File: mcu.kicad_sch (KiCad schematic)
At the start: 9 parts, among them J2 BOOT SEL, SW1 Reset Switch, U2 STM32F030F4Px

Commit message: feat: added footprints for the 5.1k resistors
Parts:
- C7: footprint Capacitor_SMD:C_0805_2012Metric_Pad1.18x1.45mm_HandSolder -> Capacitor_SMD:C_0603_1608Metric_Pad1.08x0.95mm_HandSolder
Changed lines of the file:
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@@
 			)
 		)
-		(property "Footprint" "Capacitor_SMD:C_0805_2012Metric_Pad1.18x1.45mm_HandSolder"
+		(property "Footprint" "Capacitor_SMD:C_0603_1608Metric_Pad1.08x0.95mm_HandSolder"
 			(at 267.97 43.18 0)
 			(effects

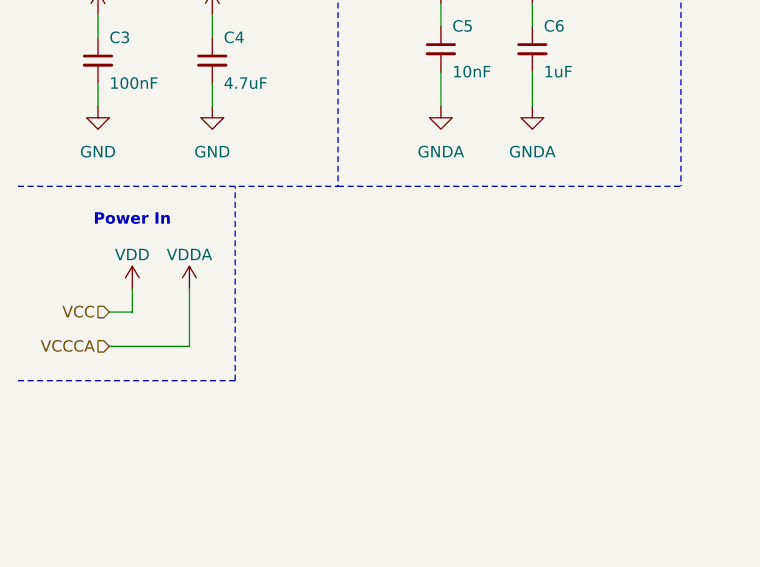
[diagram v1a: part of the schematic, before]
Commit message: feat(FT232RL_Reset): Added FT232RL Reset functionality using the Reset switch
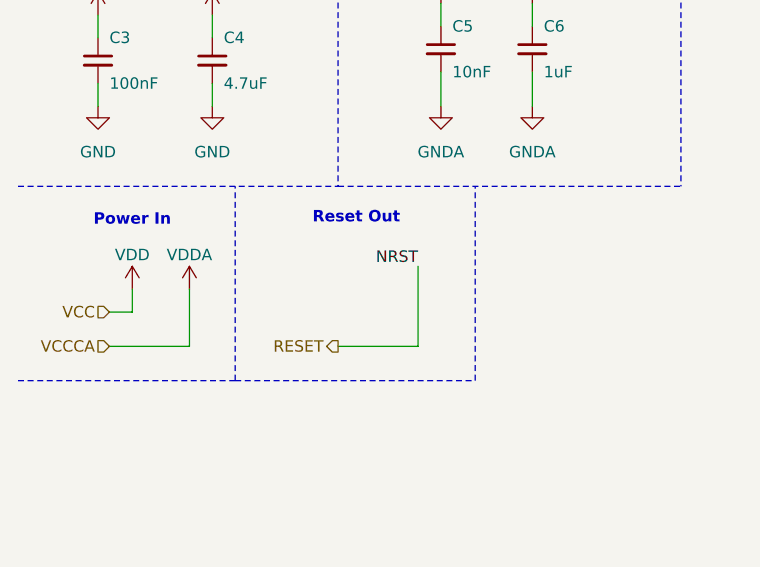
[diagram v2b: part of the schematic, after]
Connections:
- net NRST renamed RESET
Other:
- note added: "Reset Out"
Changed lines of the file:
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@@
+		)
+	)
+	(text "Reset Out\n"
+		(exclude_from_sim no)
+		(at 50.292 50.546 0)
+		(effects
+			(font
+				(size 1.27 1.27)
+				(thickness 0.254)
+				(bold yes)
+				(color 0 0 0 1)
+			)
 		)
 	)
@@
 		)
 	)
+	(polyline
+		(pts
+			(xy 63.5 68.58) (xy 63.5 46.99)
+		)
+		(stroke
+			(width 0)
+			(type dash)
+			(color 72 72 72 1)
+		)
+	)
 	(wire
 		(pts
@@
 		)
 	)
+	(polyline
+		(pts
+			(xy 36.83 68.58) (xy 63.5 68.58)
+		)
+		(stroke
+			(width 0)
+			(type dash)
+			(color 72 72 72 1)
+		)
+	)
 	(wire
 		(pts
@@
 	(wire
 		(pts
+			(xy 48.26 64.77) (xy 57.15 64.77)
+		)
+		(stroke
+			(width 0)
+			(type default)
+		)
+	)
+	(wire
+		(pts
 			(xy 241.3 38.1) (xy 229.87 38.1)
 		)
@@
 		(pts
 			(xy 218.44 38.1) (xy 224.79 38.1)
+		)
+		(stroke
+			(width 0)
+			(type default)
+		)
+	)
+	(wire
+		(pts
+			(xy 57.15 55.88) (xy 57.15 64.77)
 		)
 		(stroke
@@
 	(label "NRST"
 		(at 280.67 39.37 180)
+		(effects
+			(font
+				(size 1.27 1.27)
+			)
+			(justify right bottom)
+		)
+	)
+	(label "NRST"
+		(at 57.15 55.88 180)
 		(effects
 			(font
@@
 		)
 	)
+	(hierarchical_label "RESET"
+		(shape output)
+		(at 48.26 64.77 180)
+		(effects
+			(font
+				(size 1.27 1.27)
+			)
+			(justify right)
+		)
+	)

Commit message: feat(LED_Footprints): Added Footprints to the LEDs and its Resistors
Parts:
- R1: footprint Resistor_SMD:R_0201_0603Metric_Pad0.64x0.40mm_HandSolder -> Resistor_SMD:R_0603_1608Metric_Pad0.98x0.95mm_HandSolder
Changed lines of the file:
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@@
 			)
 		)
-		(property "Footprint" "Resistor_SMD:R_0201_0603Metric_Pad0.64x0.40mm_HandSolder"
+		(property "Footprint" "Resistor_SMD:R_0603_1608Metric_Pad0.98x0.95mm_HandSolder"
 			(at 227.33 38.1 0)
 			(effects
